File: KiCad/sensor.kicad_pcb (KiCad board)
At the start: 2 copper layers, 31.7 x 45.6 mm, 42 parts, among them J1 SKRKAEE020, J2 SKRKAEE020, J3 Conn_01x03_Male, U1 TCR2EF19, U2 LM3671MF 3.3, U3 PMW3360DM-T2QU, U4 RP2040, Y1 Crystal 3225 12MHz

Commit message: added license, some small tweaks and all.
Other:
- board text added: "MBUK Community Mouse Project Dev Kit Revision 0.3"
- board text removed: "GP19 - GP20"
- board text removed: "MBUK Community Mouse Project Dev Kit Revision 0.1"
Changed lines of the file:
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@@
     (effects (font (size 0.8 0.8) (thickness 0.15)))
   )
-  (gr_text "MBUK Community\nMouse Project\nDev Kit \nRevision 0.1" (at 121.75 94.5) (layer "F.SilkS")
+  (gr_text "MBUK Community\nMouse Project\nDev Kit \nRevision 0.3" (at 121.75 94.5) (layer "F.SilkS")
     (effects (font (size 0.7 0.7) (thickness 0.15)) (justify left))
   )
@@
     (effects (font (size 0.8 0.8) (thickness 0.15)))
   )
-  (gr_text "GP19 - GP20" (at 121.55 91.2) (layer "F.SilkS")
-    (effects (font (size 0.8 0.8) (thickness 0.15)) (justify left))
-  )
   (gr_text "GP13" (at 124.293181 133.925 90) (layer "F.SilkS")

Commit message: Decided redo PCB
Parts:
- added H1: MountingHole, MountingHole:MountingHole_2.2mm_M2, F.Cu at (70.0, 32.6)
- added H2: MountingHole, MountingHole:MountingHole_2.2mm_M2, F.Cu at (53.8, 32.6)
- added H3: MountingHole, MountingHole:MountingHole_2.2mm_M2, F.Cu at (54.0, 69.8)
- added H4: MountingHole, MountingHole:MountingHole_2.2mm_M2, F.Cu at (70.0, 70.0)
- added SW1: MouseSwitch, MouseSwitch:MouseSwitch, F.Cu at (58.0, 37.2)
- added SW2: MouseSwitch, MouseSwitch:MouseSwitch, F.Cu at (64.9, 37.2)
- C14: value 1uf 0402 -> 100nf 0402
- C16: value 100nf 0402 -> 1uf 0402
- C17: value 22pf 0402 -> 100nf 0402
- C18: value 10uf 0402 -> 22pf 0402
- C5: value 100nf 0402 -> 4.7uf 0402
- R1: value 5.1K -> 39 ohm 0402
- R3: value 200 ohm 0603 -> 10K 0402; footprint Resistor_SMD:R_0603_1608Metric -> Resistor_SMD:R_0402_1005Metric
- R4: value 1 ohm 0402 -> 5.1K
- U2: footprint Package_TO_SOT_SMD:TSOT-23-5 -> Package_TO_SOT_SMD:SOT-23-5
- moved C17 94.1 mm to (41.5, 46.8)
- moved C10 88.1 mm to (39.9, 57.9)
- moved L1 87.2 mm to (52.5, 45.3), turned to -90 degrees
- moved C1 86.8 mm to (49.4, 42.7), turned to 0 degrees
- moved D1 86.7 mm to (48.6, 40.4), turned to 90 degrees
- moved e1 86.7 mm to (46.0, 30.0)
- moved U2 86.5 mm to (49.7, 45.3), turned to 0 degrees
- moved C8 85.5 mm to (50.5, 51.6), turned to 90 degrees
- moved R6 84.8 mm to (44.5, 46.5)
- moved R7 84.7 mm to (45.5, 46.5)
- moved J1 83.8 mm to (42.0, 43.0)
- moved J2 83.7 mm to (49.6, 64.4)
- moved R2 83.3 mm to (47.2, 40.4), turned to 90 degrees
- moved R8 82.7 mm to (40.5, 50.7)
- moved FLASH1 82.4 mm to (42.3, 49.9)
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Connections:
- net VBUS renamed Net-(D1-Pad2)
- C15 pad 1: +1V1 -> +3V3
- C16 pad 1: +3V3 -> +1V1
- C17 pad 1: GND -> +3V3
- C17 pad 2: /XIN -> GND
- C18 pad 1: +3V3 -> GND
- C18 pad 2: GND -> /XIN
- C5 pad 1: +1V1 -> Net-(C5-Pad1)
- C7 pad 1: +3V3 -> +1V1
- R1 pad 1: GND -> +1V8
- R3 pad 2: /ADC_VREF -> MISO
- R4 pad 1: /ADC_VREF -> GND
- R4 pad 2: +3V3 -> Net-(R4-Pad2)
- U3 pad 10: unconnected-(U3-Pad10) -> SCLK
- U3 pad 11: unconnected-(U3-Pad11) -> MOSI
- U3 pad 12: unconnected-(U3-Pad12) -> MISO
- U3 pad 13: unconnected-(U3-Pad13) -> NCS
- U3 pad 15: unconnected-(U3-Pad15) -> Net-(R1-Pad2)
- U3 pad 3: unconnected-(U3-Pad3) -> Net-(C5-Pad1)
- U3 pad 4: unconnected-(U3-Pad4) -> +1V8
- U3 pad 5: unconnected-(U3-Pad5) -> +3V3
- U3 pad 8: unconnected-(U3-Pad8) -> GND
- U3 pad 9: unconnected-(U3-Pad9) -> MOTION
- U4 pad 12: /GPIO9 -> NCS
- U4 pad 3: /GPIO1 -> MOTION
- U4 pad 4: /GPIO2 -> SCLK
- U4 pad 5: /GPIO3 -> MOSI
- U4 pad 6: /GPIO4 -> MISO
- e1 pad 10: Net-(R2-Pad2) -> Net-(R4-Pad2)
- e1 pad 4: Net-(R1-Pad2) -> Net-(R2-Pad2)
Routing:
- net unconnected-(U3-Pad12): track 62.5 -> 0.00 mm, vias 3 -> 0
- net +1V8: track 0.00 -> 46.0 mm, vias 0 -> 1
- net /GPIO0: track 43.2 -> 0.00 mm, vias 2 -> 0
- net /GPIO1: track 40.0 -> 0.00 mm, vias 2 -> 0
- net unconnected-(U3-Pad4): track 39.8 -> 0.00 mm, vias 2 -> 0
- net /GPIO15: track 38.5 -> 0.00 mm
- net /GPIO14: track 36.2 -> 0.00 mm
- net /GPIO13: track 33.9 -> 0.00 mm
- net /GPIO12: track 31.6 -> 0.00 mm
- net unconnected-(U3-Pad13): track 30.4 -> 0.00 mm, vias 1 -> 0
- net /GPIO11: track 29.9 -> 0.00 mm
- net /GPIO10: track 28.5 -> 0.00 mm
- net /GPIO9: track 26.8 -> 0.00 mm
- net /GPIO20: track 26.5 -> 0.00 mm, vias 1 -> 0
- net /GPIO19: track 26.4 -> 0.00 mm, vias 1 -> 0
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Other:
- board size 31.7 x 45.6 mm -> 34.5 x 42.7 mm
- board text added: "MBUK Community Mouse Project Dev Kit Revision 0.4"
- board text removed: "BOOTSEL"
- board text removed: "GP10"
- board text removed: "GP11"
- board text removed: "GP12"
- board text removed: "GP13"
- board text removed: "GP14"
- board text removed: "GP15"
- board text removed: "GP2"
- board text removed: "GP4"
- board text removed: "GP5"
- board text removed: "GP7"
- board text removed: "GP8"
- board text removed: "GP9"
- board text removed: "MBUK Community Mouse Project Dev Kit Revision 0.3"
- board text removed: "RP2040"
- board text removed: "RSW"
- board text removed: "SWCLK GND SWDIO"

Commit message: Fillet :cat2:
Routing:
- net /GPIO7: track 40.2 -> 45.4 mm
- net /GPIO8: track 45.8 -> 50.7 mm
- net /GPIO5: track 29.7 -> 33.5 mm
- net /GPIO6: track 39.5 -> 43.4 mm
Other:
- board text added: "EnvOpenMouse RP2040 / PMW3360 Dev Kit Revision 0.4"
- board text removed: "MBUK Community Mouse Project Dev Kit Revision 0.4"

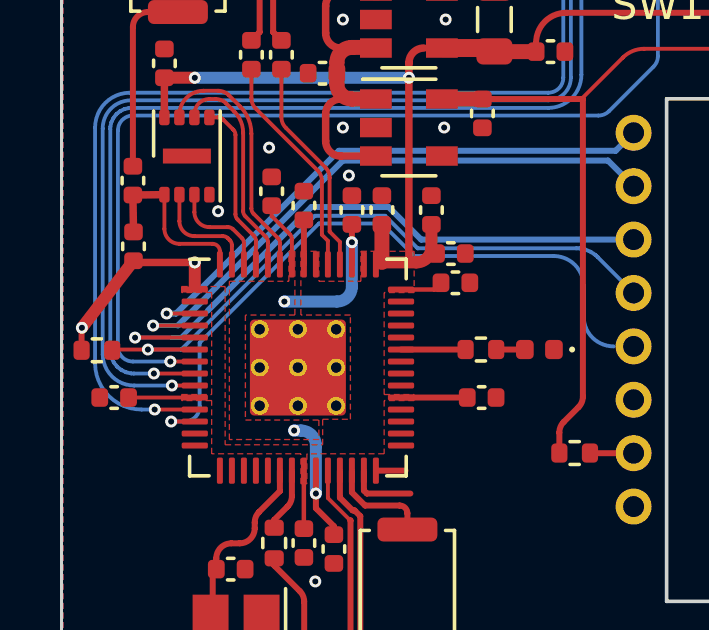
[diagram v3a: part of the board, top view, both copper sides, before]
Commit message: added rotary encoder to the schematic
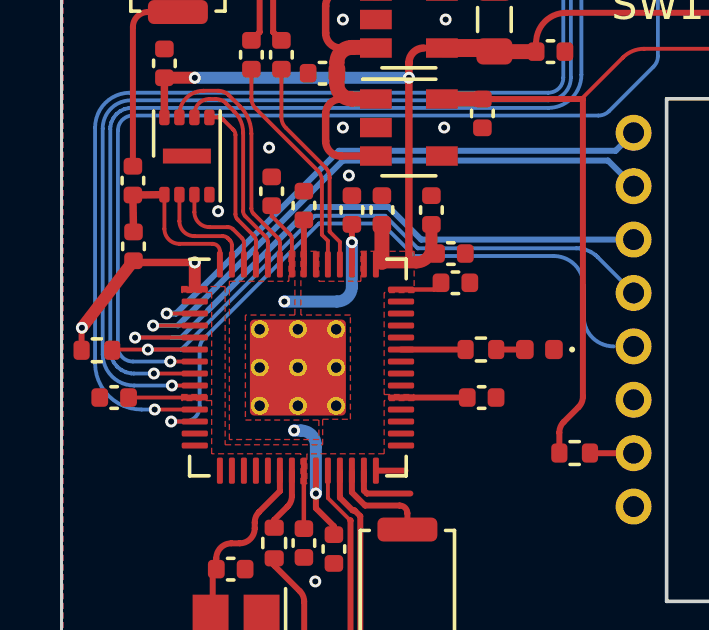
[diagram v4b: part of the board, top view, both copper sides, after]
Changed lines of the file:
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@@
   (segment (start 48.797994 52.09804) (end 49.882994 53.18304) (width 0.13) (layer "B.Cu") (net 35))
   (segment (start 55.525 54.18304) (end 55.525 55.195) (width 0.13) (layer "B.Cu") (net 35))
-  (segment (start 42.725 58.2) (end 42.725 56.075) (width 0.13) (layer "B.Cu") (net 35))
-  (segment (start 42.725 56.075) (end 46.70196 52.09804) (width 0.13) (layer "B.Cu") (net 35))
+  (segment (start 42.725 58.2) (end 42.725 56.282107) (width 0.13) (layer "B.Cu") (net 35))
+  (segment (start 42.871447 55.928553) (end 46.70196 52.09804) (width 0.13) (layer "B.Cu") (net 35))
   (segment (start 49.882994 53.18304) (end 54.525 53.18304) (width 0.13) (layer "B.Cu") (net 35))
   (segment (start 46.70196 52.09804) (end 48.797994 52.09804) (width 0.13) (layer "B.Cu") (net 35))
+  (arc (start 42.725 56.282107) (mid 42.76306 56.090765) (end 42.871447 55.928553) (width 0.13) (layer "B.Cu") (net 35))
   (arc (start 42.225 58.7) (mid 42.578553 58.553553) (end 42.725 58.2) (width 0.13) (layer "B.Cu") (net 35))
   (arc (start 54.525 53.18304) (mid 55.232107 53.475933) (end 55.525 54.18304) (width 0.13) (layer "B.Cu") (net 35))
